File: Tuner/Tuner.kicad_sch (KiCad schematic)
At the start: 12 parts, among them J1 Barrel_Jack, J2 Input, U1 STM32F411RETx, U2 NE5532, U3 AMS1117-3.3

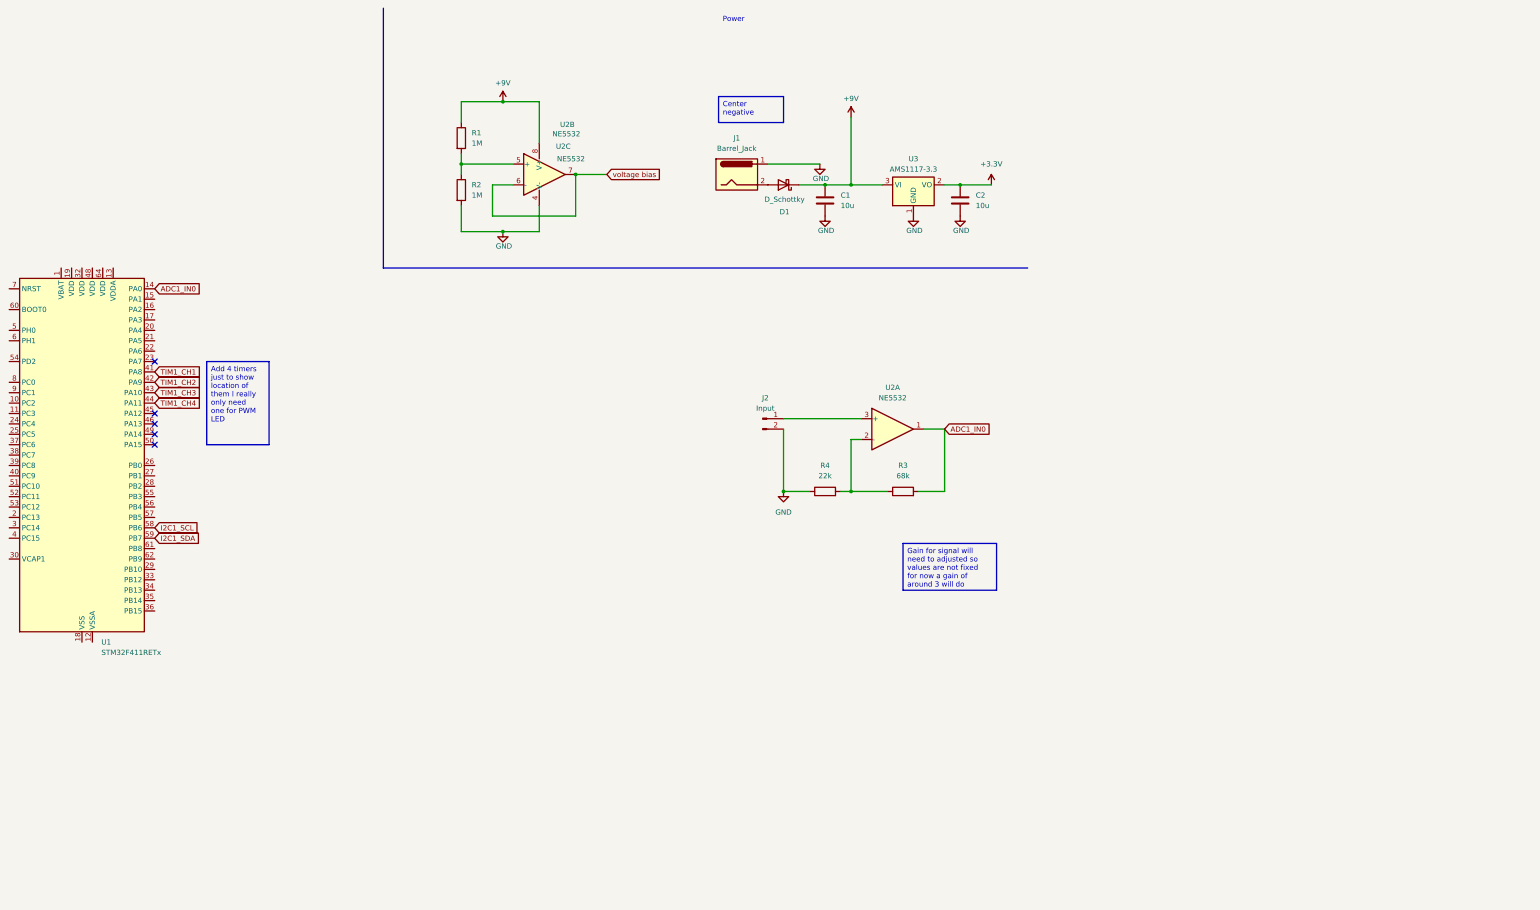
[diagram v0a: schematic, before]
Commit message: adjusted pre-amp, added digital pins for led, added LEDs drivers for LED
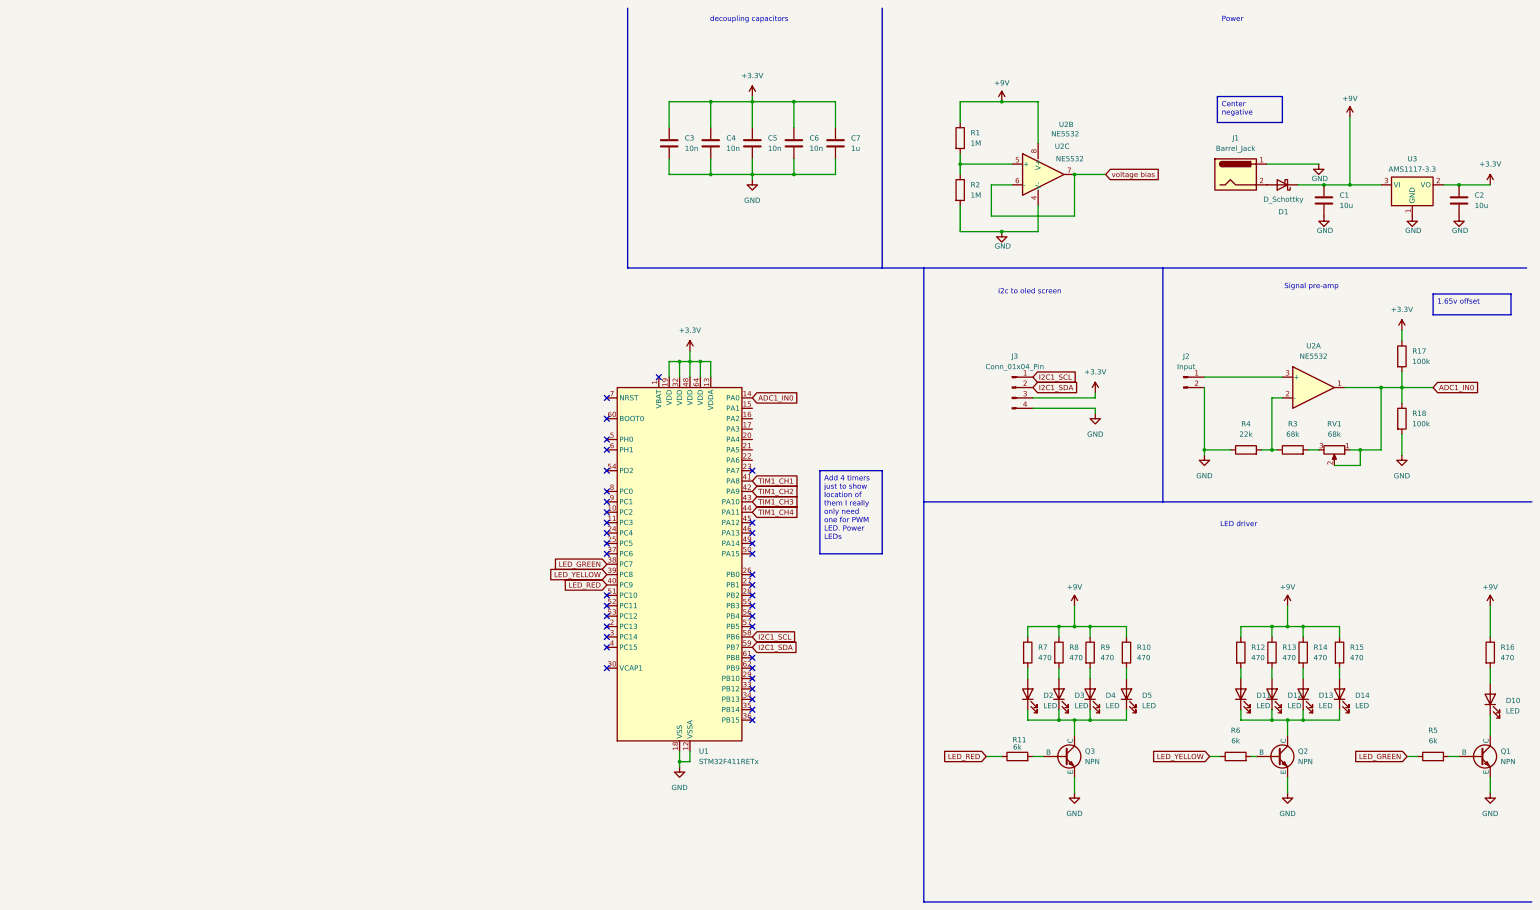
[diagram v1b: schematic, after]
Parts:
- added C3, C4, C5, C6: 10n, symbol Device:C
- added C7: 1u, symbol Device:C
- added D10, D11, D12, D13, D14, D2, D3, D4, D5: LED, symbol Device:LED
- added J3: Conn_01x04_Pin, symbol Connector:Conn_01x04_Pin
- added Q1, Q2, Q3: NPN, symbol Simulation_SPICE:NPN
- added R10, R12, R13, R14, R15, R16, R7, R8, R9: 470, symbol Device:R
- added R11, R5, R6: 6k, symbol Device:R
- added R17, R18: 100k, symbol Device:R
- added RV1: 68k, symbol Device:R_Potentiometer
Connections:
- net +3.3V: now also U1.13 (VDDA), U1.19 (VDD), U1.32 (VDD), U1.48 (VDD), U1.64 (VDD), C3.1, C4.1, C5.1, C6.1, C7.1, J3.3 (Pin_3), R17.1
- net +9V: now also R10.1, R12.1, R13.1, R14.1, R15.1, R16.1, R7.1, R8.1, R9.1
- net ADC1_IN0: now also R17.2, R18.1, RV1.1, RV1.2; no longer R3.2
- net GND: now also U1.12 (VSSA), U1.18 (VSS), U1.31 (VSS), U1.47 (VSS), U1.63 (VSS), C3.2, C4.2, C5.2, C6.2, C7.2, J3.4 (Pin_4), Q1.3 (E), Q2.3 (E), Q3.3 (E), R18.2
- net I2C1_SCL: now also J3.1 (Pin_1)
- net I2C1_SDA: now also J3.2 (Pin_2)
- net LED_GREEN: now reaches U1.38 (PC7)
- net LED_GREEN: now also R5.1
- net LED_YELLOW: now reaches U1.39 (PC8)
- net LED_YELLOW: now also R6.1
- net LED_RED: now reaches U1.40 (PC9)
- net LED_RED: now also R11.1
- new net: D2.1 (K), D3.1 (K), D4.1 (K), D5.1 (K), Q3.1 (C)
- new net: D4.2 (A), R9.2
- new net: Q1.2 (B), R5.2
- new net: Q2.2 (B), R6.2
- new net: R3.2, RV1.3
- new net: D11.1 (K), D12.1 (K), D13.1 (K), D14.1 (K), Q2.1 (C)
- new net: D11.2 (A), R12.2
- new net: D10.1 (K), Q1.1 (C)
- new net: D10.2 (A), R16.2
- new net: D5.2 (A), R10.2
- new net: D12.2 (A), R13.2
- new net: Q3.2 (B), R11.2
- new net: D13.2 (A), R14.2
- new net: D3.2 (A), R8.2
- new net: D14.2 (A), R15.2
- new net: D2.2 (A), R7.2
- no-connect marks 5 -> 38
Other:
- note added: "LED driver"
- note added: "Signal pre-amp"
- note added: "decoupling capacitors"
- note added: "i2c to oled screen"
- moved on the sheet: C1, C2, D1, J1, J2, R1, R2, R3, R4, U1, U2A, U2B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

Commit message: added 4 LEDs to the PCB and finished using the ERC to verify errors
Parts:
- added D12, D13, D14: LED, symbol Device:LED
- added J4: Conn_01x01_Pin, symbol Connector:Conn_01x01_Pin
- added R19, R20, R21: 0, symbol Device:R
- renumbered C3 to C1, C4 to C2, C5 to C3, C6 to C4, C7 to C5, C1 to C6, C2 to C7, D11 to D6, D12 to D7, D13 to D8, D14 to D9, Q3 to Q1, Q1 to Q3, R12 to R11, R13 to R12, R14 to R13, R15 to R14, R16 to R15, R11 to R16, R6 to R17, R5 to R18, R17 to R3, R18 to R4, R4 to R5, R3 to R6, U2 to U1, U3 to U2, U1 to U3
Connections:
- net GND: now also D12.1 (K), D13.1 (K), D14.1 (K), R19.2, R20.2, R21.2; no longer Q1.3 (E), Q2.3 (E), Q3.3 (E)
- net TIM1_CH1: now also J4.1 (Pin_1)
- net TIM1_CH2: now also D12.2 (A)
- net TIM1_CH3: now also D13.2 (A)
- net TIM1_CH4: now also D14.2 (A)
- new net: Q2.3 (E), R20.1
- new net: Q1.3 (E), R19.1
- new net: Q3.3 (E), R21.1
- no-connect marks 38 -> 44

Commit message: finalized some stm32 necessities
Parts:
- removed J4: Conn_01x01_Pin, symbol Connector:Conn_01x01_Pin
- added C10, C9: 8pf, Capacitor_SMD:C_0603_1608Metric_Pad1.08x0.95mm_HandSolder, symbol Device:C
- added C8: 100n, Capacitor_SMD:C_0603_1608Metric_Pad1.08x0.95mm_HandSolder, symbol Device:C
- added J4: SWD, Connector_PinHeader_2.54mm:PinHeader_2x05_P2.54mm_Vertical, symbol Connector_Generic:Conn_02x05_Odd_Even
- added J5: output channel, Connector_PinHeader_2.54mm:PinHeader_1x02_P2.54mm_Vertical, symbol Connector:Conn_01x02_Pin
- added J6: TIM1 output, Connector_PinHeader_2.54mm:PinHeader_1x02_P2.54mm_Vertical, symbol Connector:Conn_01x02_Pin
- added R7: 0, Resistor_SMD:R_0603_1608Metric_Pad0.98x0.95mm_HandSolder, symbol Device:R
- added SW1: NRST, Connector_PinHeader_2.54mm:PinHeader_1x02_P2.54mm_Vertical, symbol Switch:SW_SPST
- added SW2: SW_SPDT, Connector_PinHeader_2.54mm:PinHeader_1x02_P2.54mm_Vertical, symbol Switch:SW_SPDT
- added Y1: 16Mhz, Crystal:Crystal_SMD_3225-4Pin_3.2x2.5mm_HandSoldering, symbol Device:Crystal_GND24
- C1, C2, C3, C4, C5, C6, C7: footprint (none) -> Capacitor_SMD:C_0603_1608Metric_Pad1.08x0.95mm_HandSolder
- D1: footprint (none) -> Diode_SMD:D_0603_1608Metric_Pad1.05x0.95mm_HandSolder
- D10, D2, D3, D4, D5, D6, D7, D8, D9: footprint (none) -> LED_SMD:LED_1206_3216Metric_Pad1.42x1.75mm_HandSolder
- D11: renamed from D12; footprint (none) -> LED_SMD:LED_1206_3216Metric_Pad1.42x1.75mm_HandSolder
- D12: renamed from D13; footprint (none) -> LED_SMD:LED_1206_3216Metric_Pad1.42x1.75mm_HandSolder
- D13: renamed from D14; footprint (none) -> LED_SMD:LED_1206_3216Metric_Pad1.42x1.75mm_HandSolder
- J1, J2: footprint (none) -> Connector_PinHeader_2.54mm:PinHeader_1x02_P2.54mm_Vertical
- J3: footprint (none) -> Connector_PinHeader_2.54mm:PinHeader_1x04_P2.54mm_Vertical
- Q1, Q2, Q3: footprint (none) -> Package_TO_SOT_SMD:SOT-23
- R1, R2, R3, R4, R5, R6, RV1: footprint (none) -> Resistor_SMD:R_0603_1608Metric_Pad0.98x0.95mm_HandSolder
- R10: renamed from R9; footprint (none) -> Resistor_SMD:R_0603_1608Metric_Pad0.98x0.95mm_HandSolder
- R11: renamed from R10; footprint (none) -> Resistor_SMD:R_0603_1608Metric_Pad0.98x0.95mm_HandSolder
- R12: renamed from R11; footprint (none) -> Resistor_SMD:R_0603_1608Metric_Pad0.98x0.95mm_HandSolder
- R13: renamed from R12; footprint (none) -> Resistor_SMD:R_0603_1608Metric_Pad0.98x0.95mm_HandSolder
- R14: renamed from R13; footprint (none) -> Resistor_SMD:R_0603_1608Metric_Pad0.98x0.95mm_HandSolder
- R15: renamed from R14; footprint (none) -> Resistor_SMD:R_0603_1608Metric_Pad0.98x0.95mm_HandSolder
- R16: renamed from R15; footprint (none) -> Resistor_SMD:R_0603_1608Metric_Pad0.98x0.95mm_HandSolder
- R17: renamed from R16; footprint (none) -> Resistor_SMD:R_0603_1608Metric_Pad0.98x0.95mm_HandSolder
- R18: renamed from R17; footprint (none) -> Resistor_SMD:R_0603_1608Metric_Pad0.98x0.95mm_HandSolder
- R19: renamed from R18; footprint (none) -> Resistor_SMD:R_0603_1608Metric_Pad0.98x0.95mm_HandSolder
- R20: renamed from R19; footprint (none) -> Resistor_SMD:R_0603_1608Metric_Pad0.98x0.95mm_HandSolder
- R21: renamed from R20; footprint (none) -> Resistor_SMD:R_0603_1608Metric_Pad0.98x0.95mm_HandSolder
- R22: renamed from R21; footprint (none) -> Resistor_SMD:R_0603_1608Metric_Pad0.98x0.95mm_HandSolder
- R8: renamed from R7; footprint (none) -> Resistor_SMD:R_0603_1608Metric_Pad0.98x0.95mm_HandSolder
- R9: renamed from R8; footprint (none) -> Resistor_SMD:R_0603_1608Metric_Pad0.98x0.95mm_HandSolder
- U1: footprint (none) -> Package_DIP:DIP-8_W7.62mm
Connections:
- net +3.3V: now also J4.1 (Pin_1), SW2.3 (C)
- net GND: now also C10.2, C8.2, C9.2, J4.3 (Pin_3), J4.5 (Pin_5), J4.9 (Pin_9), J5.1 (Pin_1), J6.1 (Pin_1), SW1.1 (A), SW2.1 (A), Y1.2, Y1.4
- net TIM1_CH1: now also J6.2 (Pin_2)
- net TMS: now reaches U3.46 (PA13)
- net TMS: now also J4.2 (Pin_2)
- net TCK: now reaches U3.49 (PA14)
- net TCK: now also J4.4 (Pin_4)
- net at U3.5 (PH0): now also C9.1, Y1.1
- net TIM2_OC1: now reaches U3.50 (PA15)
- net TIM2_OC1: now also J5.2 (Pin_2)
- net at U3.6 (PH1): now also R7.1
- net BOOT0: now reaches U3.60 (BOOT0)
- net BOOT0: now also SW2.2 (B)
- net SWO: now reaches U3.62 (PB9)
- net SWO: now also J4.6 (Pin_6)
- net NRST: now reaches U3.7 (NRST)
- net NRST: now also C8.1, J4.10 (Pin_10), SW1.2 (B)
- new net: C10.1, R7.2, Y1.3
- no-connect marks 44 -> 38
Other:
- note added: "Current Limiter"
- note added: "X322516MLB4SI"
- note added: "programming/debugging and LED driver"
- moved on the sheet: D11, D12, D13

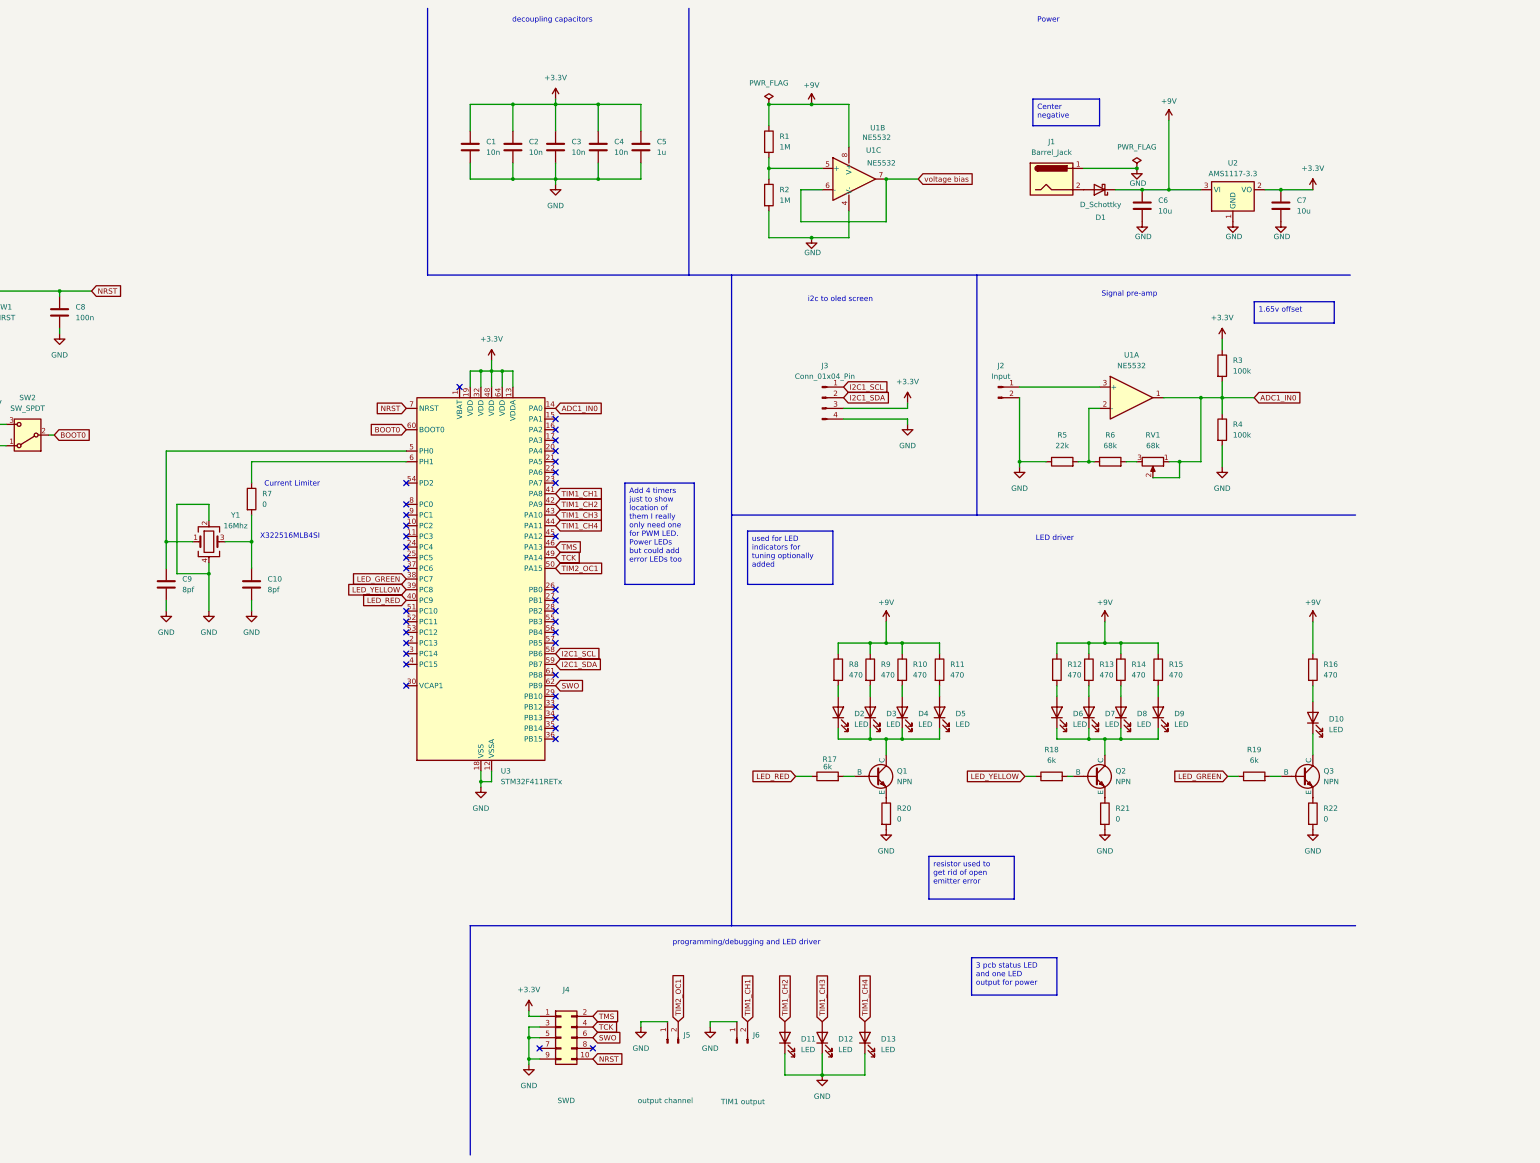
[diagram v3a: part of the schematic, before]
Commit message: revision to the schematics then grouped components together for pcb layout
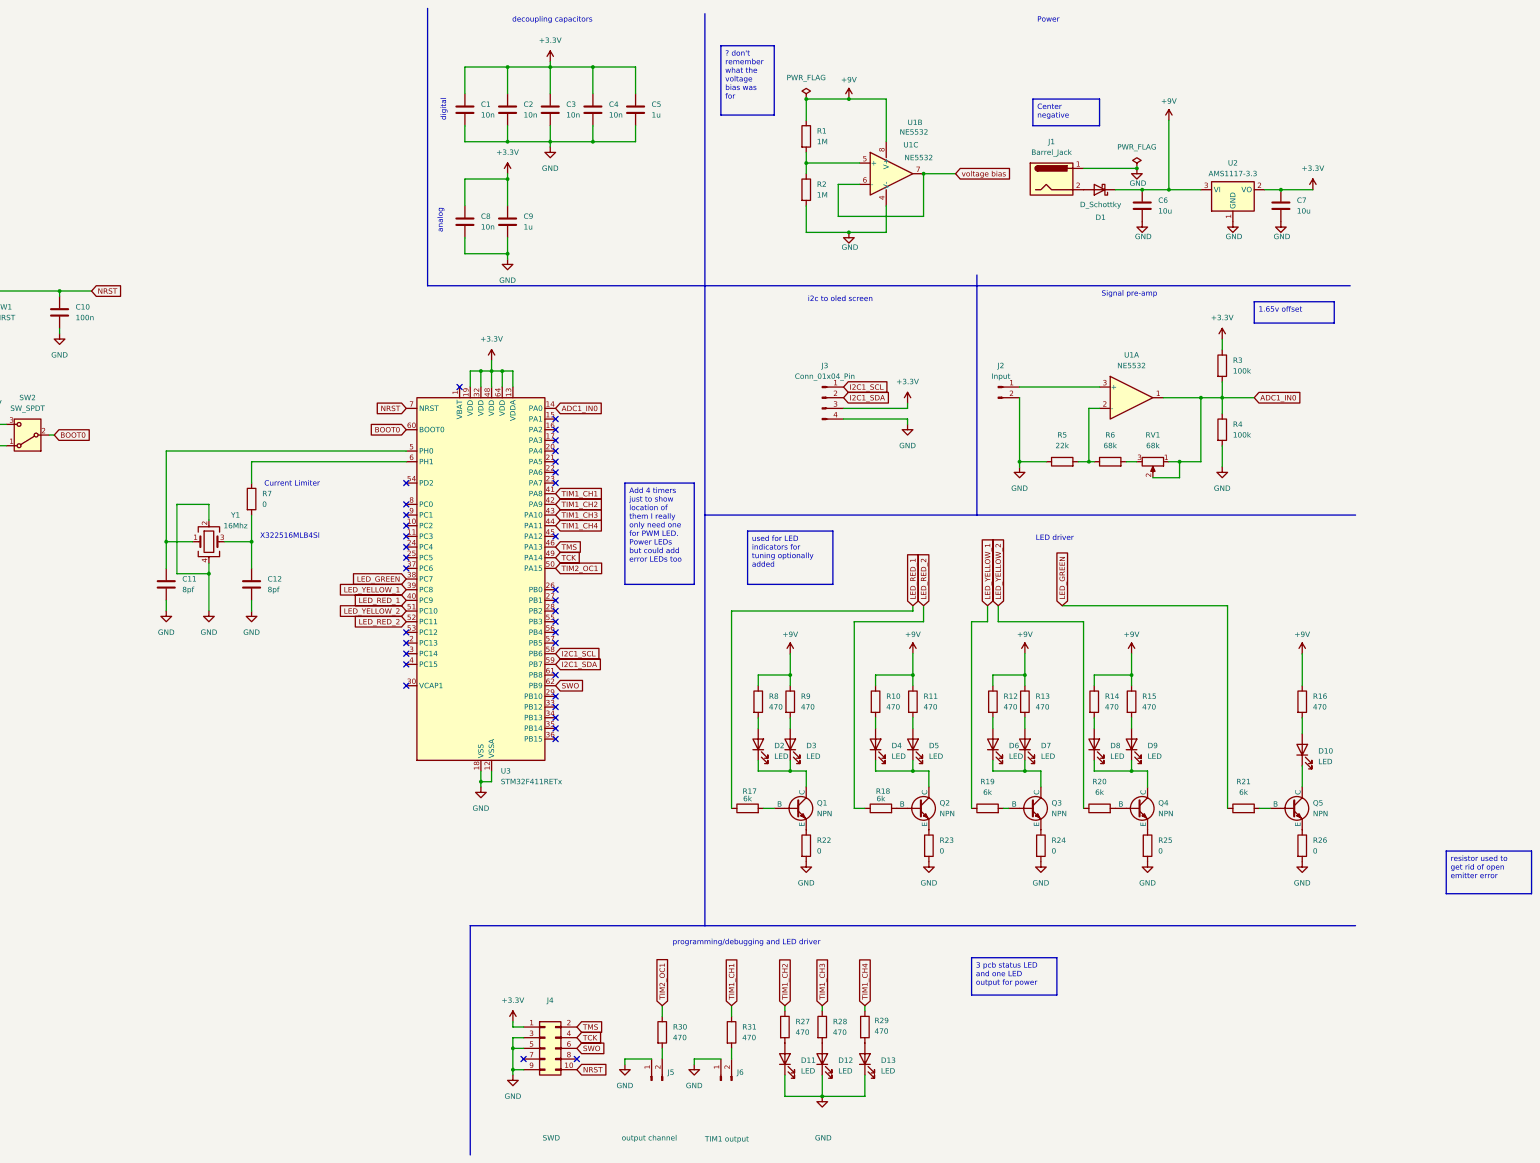
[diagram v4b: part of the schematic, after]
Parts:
- added C8: 10n, Capacitor_SMD:C_0603_1608Metric_Pad1.08x0.95mm_HandSolder, symbol Device:C
- added C9: 1u, Capacitor_SMD:C_0603_1608Metric_Pad1.08x0.95mm_HandSolder, symbol Device:C
- added Q2, Q4: NPN, Package_TO_SOT_SMD:SOT-23, symbol Simulation_SPICE:NPN
- added R18, R20: 6k, Resistor_SMD:R_0603_1608Metric_Pad0.98x0.95mm_HandSolder, symbol Device:R
- added R23, R25: 0, Resistor_SMD:R_0603_1608Metric_Pad0.98x0.95mm_HandSolder, symbol Device:R
- added R27, R28, R29, R30, R31: 470, Resistor_SMD:R_0603_1608Metric_Pad0.98x0.95mm_HandSolder, symbol Device:R
- RV1: footprint Resistor_SMD:R_0603_1608Metric_Pad0.98x0.95mm_HandSolder -> Connector_PinHeader_2.54mm:PinHeader_1x03_P2.54mm_Vertical
- SW1: footprint Connector_PinHeader_2.54mm:PinHeader_1x02_P2.54mm_Vertical -> Button_Switch_THT:SW_PUSH_6mm
- SW2: footprint Connector_PinHeader_2.54mm:PinHeader_1x02_P2.54mm_Vertical -> Button_Switch_THT:SW_E-Switch_EG2219_DPDT_Angled
- renumbered C8 to C10, C9 to C11, C10 to C12, Q2 to Q3, Q3 to Q5, R18 to R19, R19 to R21, R20 to R22, R21 to R24, R22 to R26
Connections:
- net +3.3V: now also C8.1, C9.1
- net GND: now also C8.2, C9.2, R23.2, R25.2
- net TIM1_CH1: now also R31.1; no longer J6.2 (Pin_2)
- net TIM1_CH2: now also R27.1; no longer D11.2 (A)
- net TIM1_CH3: now also R28.1; no longer D12.2 (A)
- net TIM1_CH4: now also R29.1; no longer D13.2 (A)
- net TIM2_OC1: now also R30.1; no longer J5.2 (Pin_2)
- net at D2.1 (K), D3.1 (K), Q1.1 (C): no longer D4.1 (K), D5.1 (K)
- net at D6.1 (K), D7.1 (K), Q3.1 (C): no longer D8.1 (K), D9.1 (K)
- net LED_YELLOW_2: now reaches U3.51 (PC10)
- net LED_YELLOW_2: now also R20.1
- net LED_RED_2: now reaches U3.52 (PC11)
- net LED_RED_2: now also R18.1
- net LED_RED renamed LED_RED_1
- net LED_YELLOW renamed LED_YELLOW_1
- new net: Q2.2 (B), R18.2
- new net: D4.1 (K), D5.1 (K), Q2.1 (C)
- new net: J5.2 (Pin_2), R30.2
- new net: Q4.3 (E), R25.1
- new net: D12.2 (A), R28.2
- new net: Q2.3 (E), R23.1
- new net: D11.2 (A), R27.2
- new net: Q4.2 (B), R20.2
- new net: J6.2 (Pin_2), R31.2
- new net: D13.2 (A), R29.2
- new net: D8.1 (K), D9.1 (K), Q4.1 (C)
- no-connect marks 38 -> 36
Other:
- note added: "analog"
- note added: "digital"
- moved on the sheet: C1, C2, C3, C4, C5, D10, D11, D12, D13, D2, D3, D4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
